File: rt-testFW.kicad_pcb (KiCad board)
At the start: 2 copper layers, 11 parts, among them J1 1Min, J2 2Min, J3 3Min, J4 5Min, SW1 TestStart-Peach, SW2 Reset-Black

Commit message: initial iteration complete
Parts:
- removed D1: LED, LED_THT:LED_D4.0mm
- removed J1: 1Min, Connector_PinSocket_2.54mm:PinSocket_1x02_P2.54mm_Vertical
- removed J2: 2Min, Connector_PinSocket_2.54mm:PinSocket_1x02_P2.54mm_Vertical
- removed J3: 3Min, Connector_PinSocket_2.54mm:PinSocket_1x02_P2.54mm_Vertical
- removed J4: 5Min, Connector_PinSocket_2.54mm:PinSocket_1x02_P2.54mm_Vertical
- removed R2, R3: R, Resistor_THT:R_Axial_DIN0309_L9.0mm_D3.2mm_P2.54mm_Vertical
- removed SW1: TestStart-Peach, Button_Switch_THT:SW_PUSH_6mm
- removed SW2: Reset-Black, Button_Switch_THT:SW_PUSH_6mm
- added J1-1Min1: Conn_01x02_Male, Connector_PinHeader_2.00mm:PinHeader_1x02_P2.00mm_Vertical, F.Cu at (220.3, 106.3)
- added J2-2Min1: Conn_01x02_Male, Connector_PinHeader_2.00mm:PinHeader_1x02_P2.00mm_Vertical, F.Cu at (212.1, 106.3)
- added J3-3Min1: Conn_01x02_Male, Connector_PinHeader_2.00mm:PinHeader_1x02_P2.00mm_Vertical, F.Cu at (203.8, 106.6)
- added J4-5Min1: Conn_01x02_Male, Connector_PinHeader_2.00mm:PinHeader_1x02_P2.00mm_Vertical, F.Cu at (195.4, 106.6)
- added J5-CLK-DIO1: Conn_01x02_Male, Connector_PinHeader_2.00mm:PinHeader_1x02_P2.00mm_Vertical, F.Cu at (228.3, 94.5)
- added J5-VCC-GND1: Conn_01x02_Male, Connector_PinHeader_2.00mm:PinHeader_1x02_P2.00mm_Vertical, F.Cu at (228.6, 86.6)
- added LED1: LED, Connector_PinHeader_2.00mm:PinHeader_1x02_P2.00mm_Vertical, F.Cu at (194.3, 93.6)
- added Reset-Black1: SW_Push_Dual, Button_Switch_THT:SW_PUSH_6mm, F.Cu at (181.5, 80.3)
- added TestStart-Peach1: SW_Push_Dual, Button_Switch_THT:SW_PUSH_6mm, F.Cu at (181.5, 91.7)
- R1: footprint Resistor_THT:R_Axial_DIN0309_L9.0mm_D3.2mm_P2.54mm_Vertical -> Connector_PinHeader_2.00mm:PinHeader_1x02_P2.00mm_Vertical
- moved R1 70.4 mm to (199.4, 94.0)
- moved A1 36.8 mm to (194.3, 76.5)
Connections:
- A1 pad 18: unconnected-(A1-D3-Pad18) -> Net-(A1-Pad18)
- A1 pad 20: unconnected-(A1-D5-Pad20) -> Net-(A1-Pad20)
- A1 pad 23: unconnected-(A1-D8-Pad23) -> Net-(A1-Pad23)
- A1 pad 27: unconnected-(A1-D12-Pad27) -> Net-(A1-Pad27)
- A1 pad 29: unconnected-(A1-GND-Pad29) -> Net-(A1-Pad29)
- A1 pad 7: unconnected-(A1-GND-Pad7) -> Net-(A1-Pad7)
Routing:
- net Net-(A1-Pad5): track 0.00 -> 89.7 mm
- net Net-(A1-Pad21): track 0.00 -> 68.1 mm
- net Net-(A1-Pad7): track 0.00 -> 51.3 mm
- net Net-(A1-Pad19): track 0.00 -> 45.6 mm
- net Net-(A1-Pad29): track 0.00 -> 37.9 mm
- net Net-(A1-Pad18): track 0.00 -> 36.2 mm
- net Net-(A1-Pad20): track 0.00 -> 33.2 mm
- net Net-(A1-Pad27): track 0.00 -> 22.7 mm
- net Net-(J1-1Min1-Pad1): track 0.00 -> 21.9 mm
- net Net-(A1-Pad22): track 0.00 -> 21.8 mm
- net Net-(A1-Pad23): track 0.00 -> 21.7 mm
- net Net-(A1-Pad3): track 0.00 -> 12.8 mm
- net Net-(R1-Pad1): track 0.00 -> 5.76 mm
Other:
- board text added: "10"
- board text added: "11"
- board text added: "12"
- board text added: "13"
- board text added: "2"
- board text added: "3"
- board text added: "3V3"
- board text added: "4"
- board text added: "5"
- board text added: "6"
- board text added: "7"
- board text added: "8"
- board text added: "9"
- board text added: "AREF"
- board text added: "IOR"
- board text added: "RES"
- board text added: "RX0"
- board text added: "SCL"
- board text added: "SDA"
- board text added: "TX1"
- board text removed: "3.3V"
- board text removed: "D10"
- board text removed: "D11"
- board text removed: "D12"
- board text removed: "D13"
- board text removed: "D14"
- board text removed: "D15"
- board text removed: "D16"
- board text removed: "D17"
- board text removed: "D2"
- board text removed: "D3"
- board text removed: "D4"
- board text removed: "D5"
- board text removed: "D6"
- board text removed: "D7"
- board text removed: "D8"
- board text removed: "D9"
- board text removed: "IOREF"
- board text removed: "RESET"
- board text removed: "RX"
- board text removed: "TX"

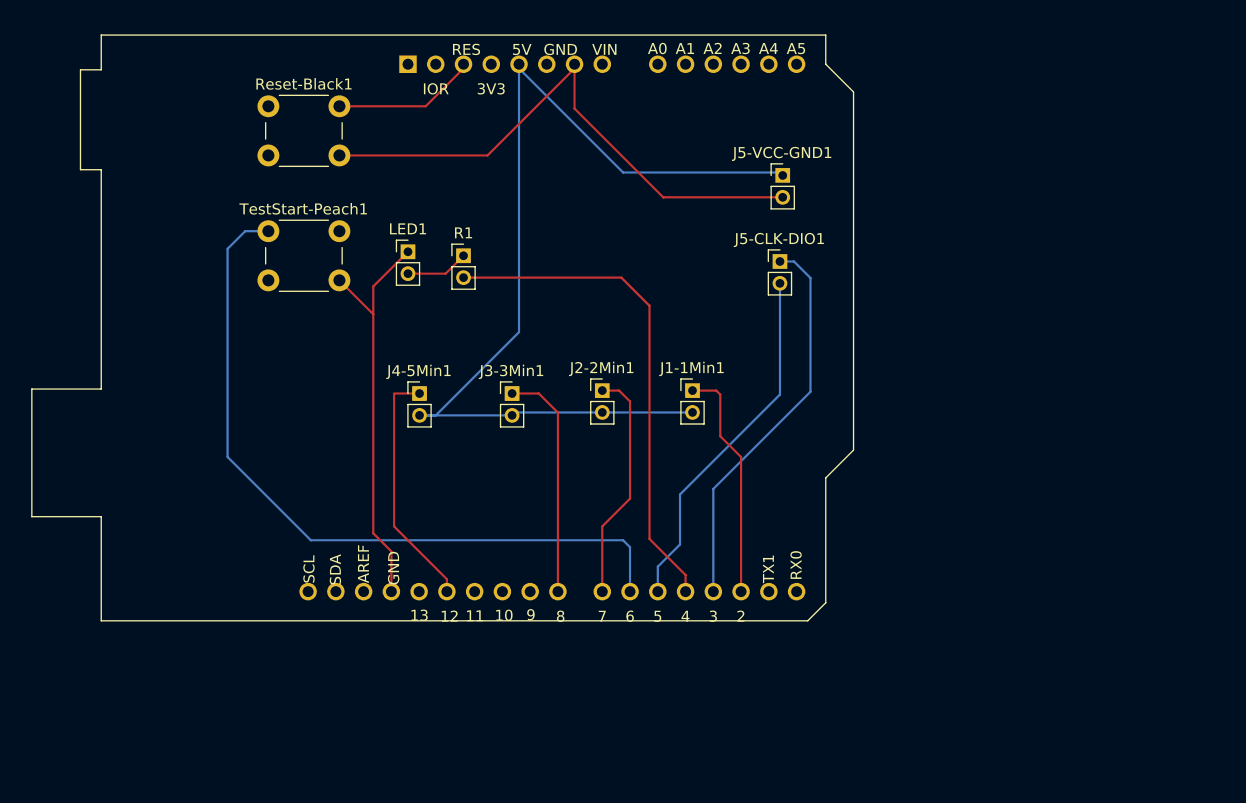
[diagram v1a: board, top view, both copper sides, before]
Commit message: final update to support tm1637 digital output
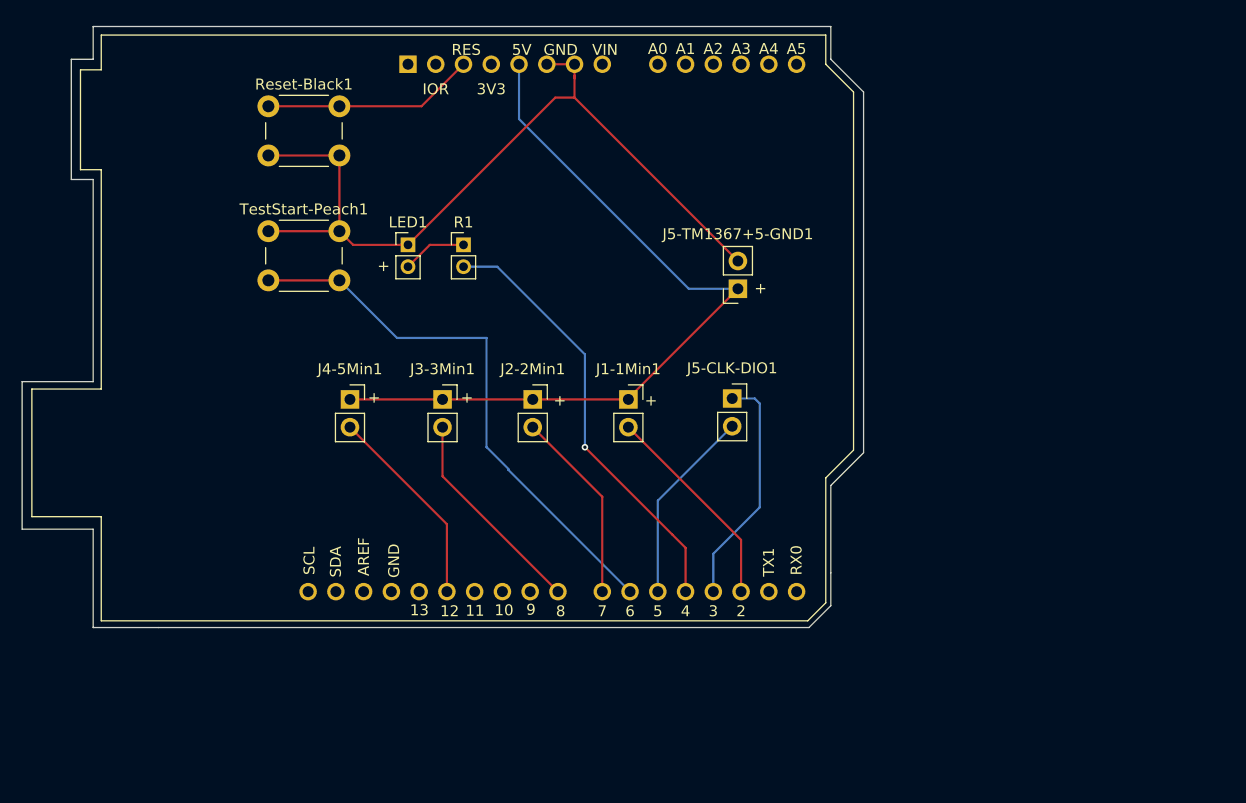
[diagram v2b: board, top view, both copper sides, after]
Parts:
- removed J5-VCC-GND1: Conn_01x02_Male, Connector_PinHeader_2.00mm:PinHeader_1x02_P2.00mm_Vertical
- added J5-TM1367+5-GND1: Conn_01x02_Male, Connector_PinSocket_2.54mm:PinSocket_1x02_P2.54mm_Vertical, F.Cu at (224.5, 97.0)
- J1-1Min1, J2-2Min1, J3-3Min1, J4-5Min1, J5-CLK-DIO1: footprint Connector_PinHeader_2.00mm:PinHeader_1x02_P2.00mm_Vertical -> Connector_PinSocket_2.54mm:PinSocket_1x02_P2.54mm_Vertical
- moved J5-CLK-DIO1 13.3 mm to (224.0, 107.0)
- moved J2-2Min1 6.42 mm to (205.7, 107.1)
- moved J3-3Min1 6.39 mm to (197.5, 107.1)
- moved J4-5Min1 6.39 mm to (189.0, 107.1)
- moved J1-1Min1 5.93 mm to (214.5, 107.1)
- moved R1 1.00 mm to (199.4, 93.0)
- moved LED1 0.63 mm to (194.3, 93.0)
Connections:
- A1 pad 17: Net-(J1-1Min1-Pad1) -> Net-(A1-D2)
- A1 pad 21: Net-(A1-Pad21) -> Net-(A1-D6)
- A1 pad 22: Net-(A1-Pad22) -> Net-(A1-D7)
- A1 pad 23: Net-(A1-Pad23) -> Net-(A1-D8)
- A1 pad 27: Net-(A1-Pad27) -> Net-(A1-D12)
- A1 pad 29: Net-(A1-Pad29) -> GND
- A1 pad 5: Net-(A1-Pad5) -> +5V
- A1 pad 6: unconnected-(A1-Pad6) -> GND
- A1 pad 7: Net-(A1-Pad7) -> GND
- J1-1Min1 pad 1: Net-(J1-1Min1-Pad1) -> +5V
- J1-1Min1 pad 2: Net-(A1-Pad5) -> Net-(A1-D2)
- J2-2Min1 pad 1: Net-(A1-Pad22) -> +5V
- J2-2Min1 pad 2: Net-(A1-Pad5) -> Net-(A1-D7)
- J3-3Min1 pad 1: Net-(A1-Pad23) -> +5V
- J3-3Min1 pad 2: Net-(A1-Pad5) -> Net-(A1-D8)
- J4-5Min1 pad 1: Net-(A1-Pad27) -> +5V
- J4-5Min1 pad 2: Net-(A1-Pad5) -> Net-(A1-D12)
- LED1 pad 1: Net-(A1-Pad29) -> GND
- Reset-Black1 pad 2: Net-(A1-Pad7) -> GND
- TestStart-Peach1 pad 1: Net-(A1-Pad21) -> GND
- TestStart-Peach1 pad 2: Net-(A1-Pad29) -> Net-(A1-D6)
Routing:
- net Net-(A1-Pad5): track 89.7 -> 0.00 mm
- net GND: track 0.00 -> 74.5 mm
- net +5V: track 0.00 -> 71.2 mm
- net Net-(A1-Pad21): track 68.1 -> 0.00 mm
- net Net-(A1-Pad7): track 51.3 -> 0.00 mm
- net Net-(A1-D6): track 0.00 -> 50.8 mm
- net Net-(A1-Pad29): track 37.9 -> 0.00 mm
- net Net-(A1-Pad27): track 22.7 -> 0.00 mm
- net Net-(J1-1Min1-Pad1): track 21.9 -> 0.00 mm
- net Net-(A1-Pad22): track 21.8 -> 0.00 mm
- net Net-(A1-Pad23): track 21.7 -> 0.00 mm
- net Net-(A1-D8): track 0.00 -> 19.4 mm
- net Net-(A1-D2): track 0.00 -> 19.3 mm
- net Net-(A1-D12): track 0.00 -> 18.7 mm
- net Net-(A1-D7): track 0.00 -> 17.7 mm
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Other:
- board outline added: 77 x 55 mm
- board text added: "+"

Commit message: added label with version to pcb
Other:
- board text added: "Regatta Timer Test Framework v0.5.0"
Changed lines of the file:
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@@
+		)
+	)
+	(gr_text "Regatta Timer\nTest Framework v0.5.0"
+		(at 170 96.5 90)
+		(layer "F.SilkS")
+		(effects
+			(font
+				(size 1 1)
+				(thickness 0.1)
+			)
+			(justify bottom)
 		)
 	)

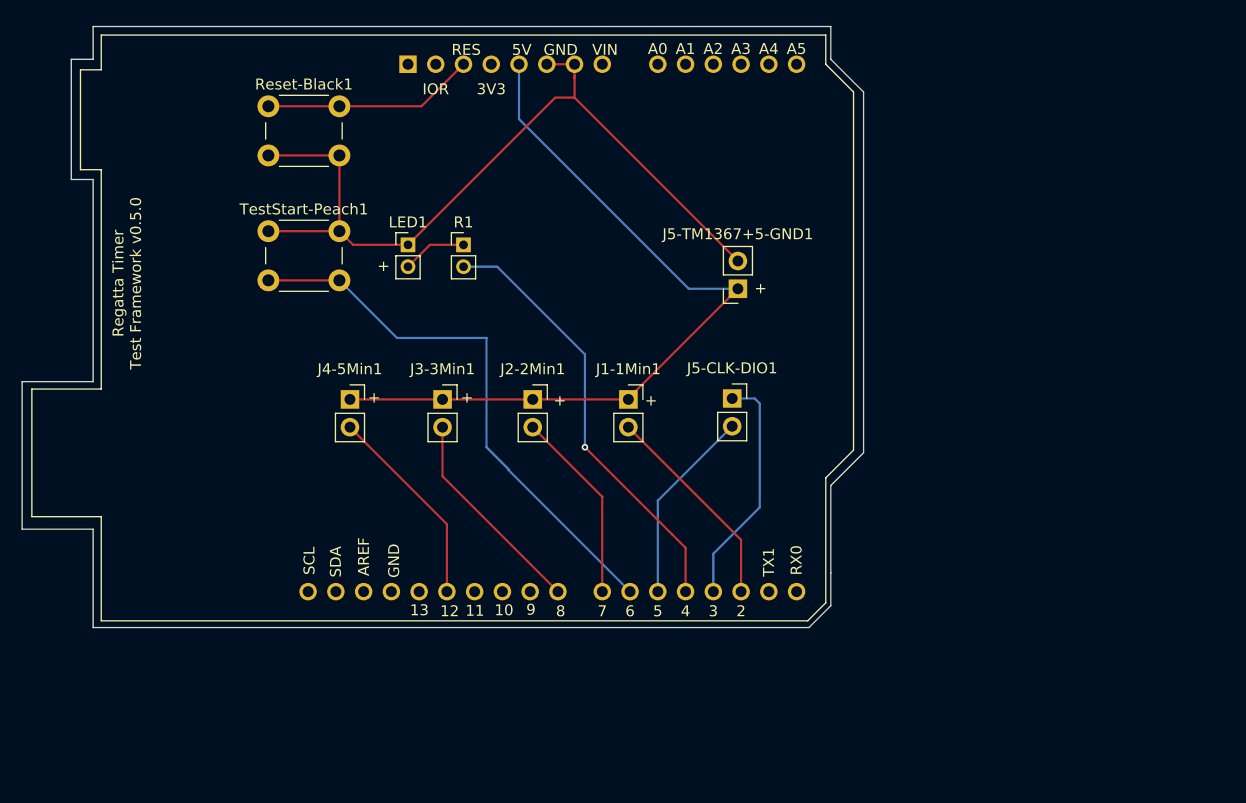
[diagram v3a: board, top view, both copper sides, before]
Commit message: pcb-flip complete, add custom uno library
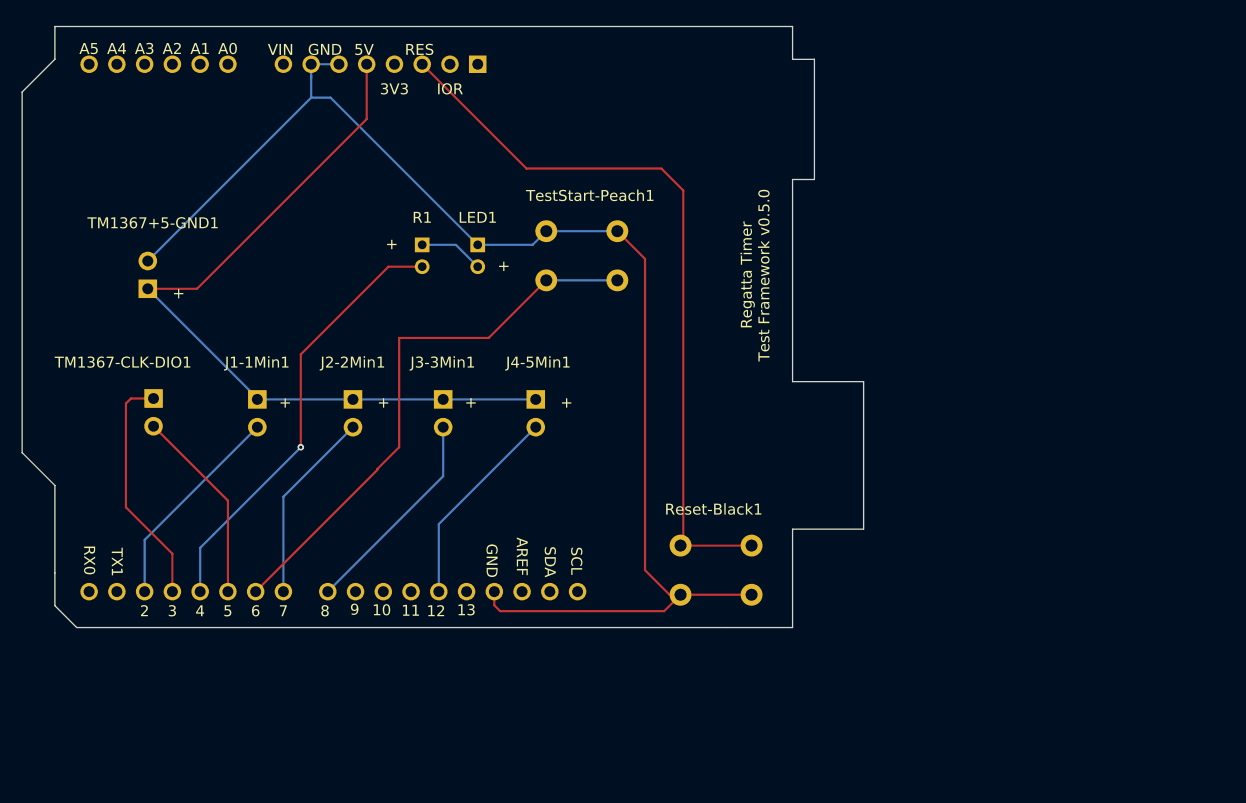
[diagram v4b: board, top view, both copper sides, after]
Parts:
- A1: footprint Module:Arduino_UNO_R3 -> KiCad-Library:Arduino_UNO_R3; moved to B.Cu
- J1-1Min1, J2-2Min1, J3-3Min1, J4-5Min1, LED1, R1, Reset-Black1, TestStart-Peach1: moved to B.Cu
- TM1367+5-GND1: renamed from J5-TM1367+5-GND1; moved to B.Cu
- TM1367-CLK-DIO1: renamed from J5-CLK-DIO1; moved to B.Cu
- moved Reset-Black1 59.8 mm to (225.8, 120.5), turned to 180 degrees
- moved TM1367+5-GND1 54.0 mm to (170.5, 97.0), turned to 0 degrees
- moved TM1367-CLK-DIO1 52.9 mm to (171.0, 107.0), turned to 180 degrees
- moved J1-1Min1 33.9 mm to (180.5, 107.1), turned to 180 degrees
- moved TestStart-Peach1 31.9 mm to (213.5, 91.7), turned to 180 degrees
- moved J4-5Min1 17.0 mm to (206.0, 107.1), turned to 180 degrees
- moved J2-2Min1 16.4 mm to (189.3, 107.1), turned to 180 degrees
- moved A1 6.38 mm to (200.7, 76.5), turned to 180 degrees
- moved LED1 6.38 mm to (200.7, 93.0), turned to 180 degrees
- moved R1 3.78 mm to (195.6, 93.0), turned to 180 degrees
- moved J3-3Min1 0.06 mm to (197.5, 107.1), turned to 180 degrees
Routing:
- net GND: track 74.5 -> 123.0 mm
- net Net-(A1-~{RESET}): track 19.4 -> 67.8 mm
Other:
- outline, holes or cut-outs redrawn

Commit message: pcb relayout complete
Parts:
- removed TM1367+5-GND1, TM1367-CLK-DIO1: Conn_01x02_Male, Connector_PinSocket_2.54mm:PinSocket_1x02_P2.54mm_Vertical
- added J5-CLK-DIO1: Conn_01x02_Male, Connector_PinSocket_2.54mm:PinSocket_1x02_P2.54mm_Vertical, F.Cu at (177.1, 94.4)
- added J5-TM1367+5-GND1: Conn_01x02_Male, Connector_PinSocket_2.54mm:PinSocket_1x02_P2.54mm_Vertical, F.Cu at (177.3, 85.5)
- A1, J1-1Min1, J2-2Min1, J3-3Min1, J4-5Min1, LED1, R1, Reset-Black1, TestStart-Peach1: moved to F.Cu
- moved TestStart-Peach1 15.4 mm to (207.5, 105.9), turned to 0 degrees
- moved LED1 14.1 mm to (213.9, 97.8), turned to 0 degrees
- moved R1 11.7 mm to (206.3, 97.8), turned to 0 degrees
- moved J1-1Min1 10.5 mm to (170.1, 106.2), turned to 0 degrees
- moved J2-2Min1 8.75 mm to (180.6, 106.2), turned to 0 degrees
- moved J4-5Min1 8.72 mm to (197.3, 106.2), turned to 0 degrees
- moved J3-3Min1 8.63 mm to (188.9, 106.2), turned to 0 degrees
- moved Reset-Black1 6.02 mm to (219.8, 120.0), turned to 0 degrees
- moved A1 0.97 mm to (200.6, 75.5), turned to 0 degrees
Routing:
- net GND: track 123.0 -> 136.2 mm
- net Net-(A1-D6): track 50.8 -> 40.2 mm
- net Net-(A1-D3): track 21.7 -> 31.2 mm
- net Net-(A1-D5): track 18.0 -> 27.1 mm
- net Net-(A1-D4): track 40.0 -> 45.1 mm, vias 1 -> 0
- net +5V: track 71.2 -> 66.6 mm
- net Net-(A1-D2): track 19.3 -> 15.0 mm
- net Net-(A1-D12): track 18.7 -> 15.1 mm
- net Net-(A1-D8): track 19.4 -> 15.9 mm
- net Net-(LED1-A): track 5.91 -> 8.51 mm
- net Net-(A1-D7): track 17.7 -> 15.9 mm
- net Net-(A1-~{RESET}): track 67.8 -> 66.3 mm
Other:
- board size 77 x 55 mm -> 75.8 x 54.1 mm
- board text added: "Regatta Timer Test Framework v1.0.0"
- board text removed: "+"
- board text removed: "10"
- board text removed: "11"
- board text removed: "12"
- board text removed: "13"
- board text removed: "2"
- board text removed: "3"
- board text removed: "3V3"
- board text removed: "4"
- board text removed: "5"
- board text removed: "5V"
- board text removed: "6"
- board text removed: "7"
- board text removed: "8"
- board text removed: "9"
- board text removed: "A0"
- board text removed: "A1"
- board text removed: "A2"
- board text removed: "A3"
- board text removed: "A4"
- board text removed: "A5"
- board text removed: "AREF"
- board text removed: "GND"
- board text removed: "IOR"
- board text removed: "RES"
- board text removed: "RX0"
- board text removed: "Regatta Timer Test Framework v0.5.0"
- board text removed: "SCL"
- board text removed: "SDA"
- board text removed: "TX1"
- board text removed: "VIN"

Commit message: partial commit to save work
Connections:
- J1-1Min1 pad 1: +5V -> GND
- J2-2Min1 pad 1: +5V -> GND
- J3-3Min1 pad 1: +5V -> GND
- J4-5Min1 pad 1: +5V -> GND
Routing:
- net +5V: track 66.6 -> 18.2 mm
- net GND: track 136.2 -> 169.2 mm
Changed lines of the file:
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@@
 			(layers "*.Cu" "*.Mask")
 			(remove_unused_layers no)
-			(net 12 "+5V")
+			(net 1 "GND")
 			(pinfunction "Pin_1")
 			(pintype "passive")
@@
 			(layers "*.Cu" "*.Mask")
 			(remove_unused_layers no)
-			(net 12 "+5V")
+			(net 1 "GND")
 			(pinfunction "Pin_1")
 			(pintype "passive")
@@
 			(layers "*.Cu" "*.Mask")
 			(remove_unused_layers no)
-			(net 12 "+5V")
+			(net 1 "GND")
 			(pinfunction "Pin_1")
 			(pintype "passive")
@@
 			(layers "*.Cu" "*.Mask")
 			(remove_unused_layers no)
-			(net 12 "+5V")
+			(net 1 "GND")
 			(pinfunction "Pin_1")
 			(pintype "passive")
@@
 	(gr_poly
 		(pts
-			(xy 235.3 105) (xy 235.3 117.2) (xy 235.3 117.2) (xy 229 117.2) (xy 229 117.2) (xy 229 126.6) (xy 229 126.6)
-			(xy 163.8 126.7) (xy 162 124.9) (xy 162 113.4) (xy 162 113.4) (xy 162 113.4) (xy 159.5 110.9) (xy 159.5 78)
-			(xy 162.1 75.3) (xy 162.1 75.3) (xy 162.1 75.3) (xy 162.1 72.6) (xy 162.1 72.6) (xy 228.9 72.6) (xy 228.9 72.6)
-			(xy 228.9 75.7) (xy 228.9 75.7) (xy 230.9 75.7) (xy 230.9 85.5) (xy 230.9 85.5) (xy 228.9 85.5) (xy 228.9 85.5)
-			(xy 228.9 105) (xy 228.9 105)
+			(xy 235.3 105) (xy 235.3 117.2) (xy 229 117.2) (xy 229 126.6) (xy 163.8 126.7) (xy 162 124.9) (xy 162 113.4)
+			(xy 159.5 110.9) (xy 159.5 78) (xy 162.1 75.3) (xy 162.1 72.6) (xy 228.9 72.6) (xy 228.9 75.7) (xy 230.9 75.7)
+			(xy 230.9 85.5) (xy 228.9 85.5) (xy 228.9 105)
 		)
 		(stroke
@@
 	)
 	(segment
+		(start 202.13 109.57)
+		(end 198.76 106.2)
+		(width 0.2)
+		(layer "F.Cu")
+		(net 1)
+	)
+	(segment
+		(start 197.325 106.2)
+		(end 188.95 106.2)
+		(width 0.2)
+		(layer "F.Cu")
+		(net 1)
+	)
+	(segment
 		(start 185.37 75.49)
 		(end 187.91 75.49)
@@
 	)
 	(segment
+		(start 180.575 106.2)
+		(end 188.95 106.2)
+		(width 0.2)
+		(layer "F.Cu")
+		(net 1)
+	)
+	(segment
 		(start 219.75 124.5)
 		(end 226.25 124.5)
@@
 	)
 	(segment
+		(start 198.76 106.2)
+		(end 197.725 106.2)
+		(width 0.2)
+		(layer "F.Cu")
+		(net 1)
+	)
+	(segment
 		(start 217.8 105.2)
 		(end 217.8 98.9)
@@
 	)
 	(segment
+		(start 170.1 106.2)
+		(end 180.575 106.2)
+		(width 0.2)
+		(layer "B.Cu")
+		(net 1)
+	)
+	(segment
 		(start 213.9 94.3)
 		(end 213.9 97.8)
@@
 	)
 	(segment
-		(start 197.325 106.2)
-		(end 188.95 106.2)
-		(width 0.2)
-		(layer "F.Cu")
-		(net 12)
-	)
-	(segment
-		(start 180.575 106.2)
-		(end 188.95 106.2)
-		(width 0.2)
-		(layer "F.Cu")
-		(net 12)
-	)
-	(segment
-		(start 180.575 87.025)
-		(end 180.575 106.2)
-		(width 0.2)
-		(layer "F.Cu")
-		(net 12)
-	)
-	(segment
-		(start 181.85 85.55)
-		(end 190.45 76.95)
-		(width 0.2)
-		(layer "F.Cu")
-		(net 12)
-	)
-	(segment
-		(start 181.85 85.75)
-		(end 180.575 87.025)
+		(start 190.5 75.54)
+		(end 190.45 75.49)
 		(width 0.2)
 		(layer "F.Cu")
@@
 	(segment
 		(start 181.85 85.55)
-		(end 181.85 85.75)
+		(end 190.5 76.9)
 		(width 0.2)
 		(layer "F.Cu")
@@
 	)
 	(segment
-		(start 190.45 76.95)
-		(end 190.45 75.49)
+		(start 190.5 76.9)
+		(end 190.5 75.54)
 		(width 0.2)
 		(layer "F.Cu")
@@
 		(net 12)
 	)
-	(segment
-		(start 170.1 106.2)
-		(end 180.575 106.2)
-		(width 0.2)
-		(layer "B.Cu")
-		(net 12)
-	)
